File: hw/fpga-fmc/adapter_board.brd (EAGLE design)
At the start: 69 x 84 mm, 5 parts, among them J1 5569262-1, J2 ASP-134488-01

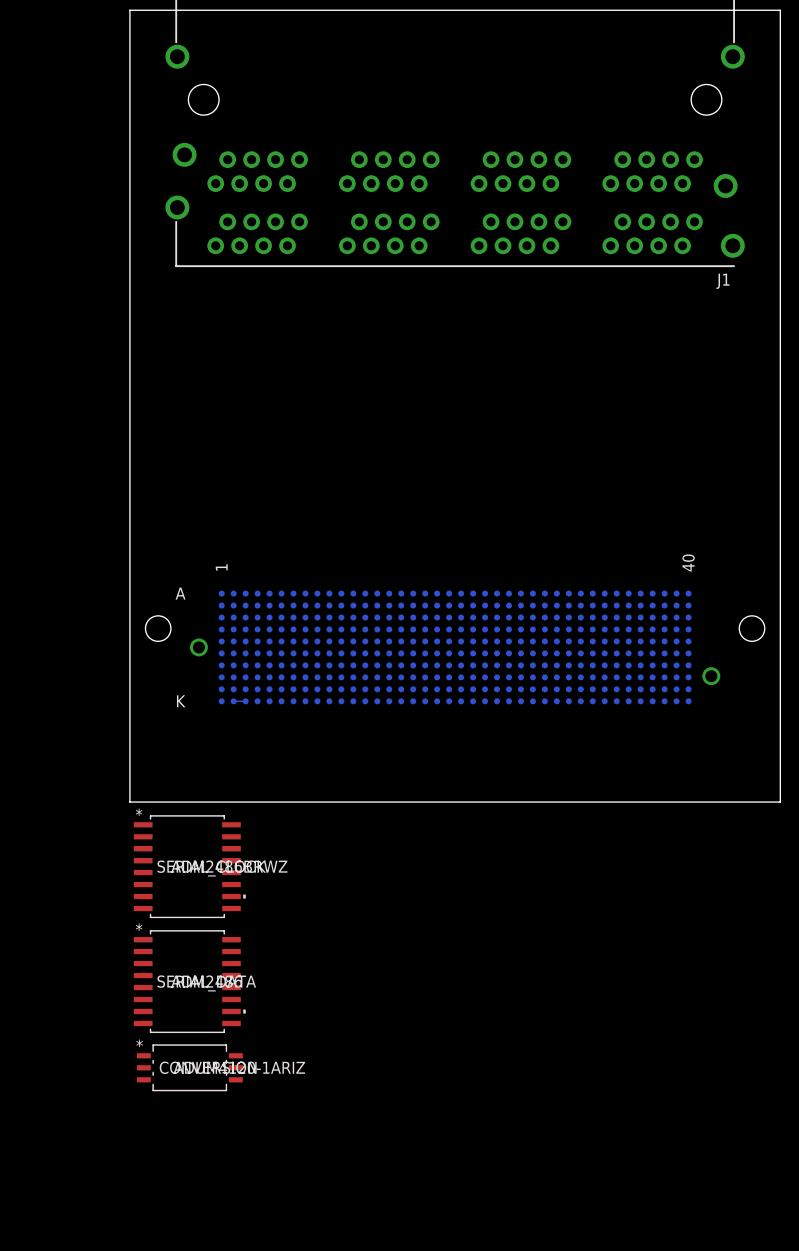
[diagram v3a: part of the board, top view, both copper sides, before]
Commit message: fpga-fmc: add more isolator ics. add i2c switch ic
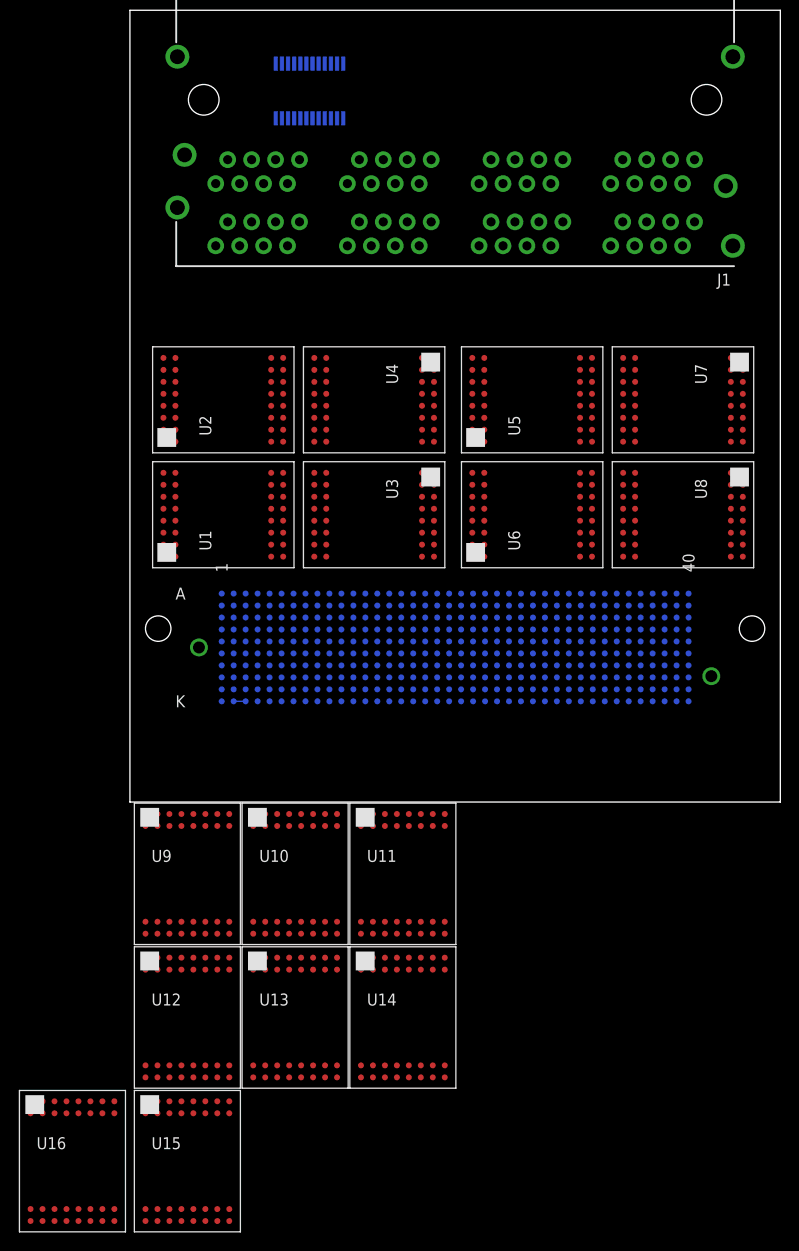
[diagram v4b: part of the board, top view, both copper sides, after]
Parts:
- removed CONVERSION: ADUM4120-1ARIZ, ADUM4120:RI_6_1_ADI
- removed SERIAL_CLOCK: ADM2486BRWZ, ADM2486:RW_16_ADI
- removed SERIAL_DATA: ADM2486, ADM2486:RW_16_ADI
- added U$1: PCA9548A, parts:PCA9548
- added U1, U10, U11, U12, U13, U14, U15, U16, U2, U3, U4, U5, U6, U7, U8, U9: LTM2881, parts:LTM2881-BGA32
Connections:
- removed net N$24: CONVERSION.5
- new net 1V8: U1.A7
- new net N$18: U1.A5
- new net N$19: U1.A2
- new net N$20: U1.A4
- new net N$23: U1.A1
- new net N$25: U1.L7, U1.L8
- new net N$30: U1.L6
- new net N$38: U1.L5
- new net N$41: U1.L3
- new net N$42: U1.L4
- new net N$43: U1.L2
- new net N$44: U1.L1
- new net N$45: U1.K1, U1.K2, U1.K3, U1.K4, U1.K5, U1.K6, U1.K7, U1.K8
- new net U1_ON: U1.A8
- net +3V3: now also U1.B6, U1.B7, U1.B8
- net 0V: now also U1.B1, U1.B2, U1.B3, U1.B4, U1.B5
- net FMC_LA06_N: now also U1.A3
- net FMC_LA06_P: now also U1.A6

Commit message: fpga-fmc: add 4 channel isolator ic
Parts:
- added I2C: ADUM1251, ADUM1251WARZ:R_8_ADI
- added U$2, U$3: ADUM140DQSOP-16, parts:QSOP16
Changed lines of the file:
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@@
 <attribute name="VALUE" x="24.506665625" y="79.248" size="1.27" layer="28" rot="MR270"/>
+</element>
+<element name="I2C" library="ADUM1251WARZ" package="R_8_ADI" value="ADUM1251" x="9.906" y="52.578" smashed="yes" rot="R90">
+<attribute name="BUILT_BY" value="EMA_UL_Team" x="9.906" y="52.578" size="1.778" layer="27" rot="R90" display="off"/>
+<attribute name="COPYRIGHT" value="Copyright (C) 2018 Accelerated Designs. All rights reserved" x="9.906" y="52.578" size="1.778" layer="27" rot="R90" display="off"/>
+<attribute name="DIGIKEY" value="ADUM1251ARZ-RL7TR-ND" x="9.906" y="52.578" size="1.778" layer="27" rot="R90" display="off"/>
+<attribute name="MANUFACTURER_PART_NUMBER" value="ADUM1251WARZ" x="9.906" y="52.578" size="1.778" layer="27" rot="R90" display="off"/>
+<attribute name="NAME" x="10.541" y="49.3014" size="1.27" layer="25" ratio="6" rot="SR90"/>
+<attribute name="SOURCELIBRARY" value="Analog_2019-03-08" x="9.906" y="52.578" size="1.778" layer="27" rot="R90" display="off"/>
+<attribute name="VALUE" x="10.541" y="50.8508" size="1.27" layer="21" ratio="6" rot="SR90"/>
+<attribute name="VENDOR" value="Analog Devices Inc" x="9.906" y="52.578" size="1.778" layer="27" rot="R90" display="off"/>
+</element>
+<element name="U$2" library="parts" package="QSOP16" package3d_urn="urn:adsk.eagle:package:3955/1" value="ADUM140DQSOP-16" x="42.672" y="52.578" smashed="yes">
+<attribute name="NAME" x="39.632" y="50.038" size="1.27" layer="25" rot="R90"/>
+<attribute name="VALUE" x="46.982" y="50.038" size="1.27" layer="27" rot="R90"/>
+</element>
+<element name="U$3" library="parts" package="QSOP16" package3d_urn="urn:adsk.eagle:package:3955/1" value="ADUM140DQSOP-16" x="25.908" y="52.578" smashed="yes">
+<attribute name="NAME" x="22.868" y="50.038" size="1.27" layer="25" rot="R90"/>
+<attribute name="VALUE" x="30.218" y="50.038" size="1.27" layer="27" rot="R90"/>
 </element>
 </elements>
@@
 </drawing>
 <compatibility>
+<note version="8.3" severity="warning">
+Since Version 8.3, EAGLE supports URNs for individual library
+assets (packages, symbols, and devices). The URNs of those assets
+will not be understood (or retained) with this version.
+</note>
+<note version="8.3" severity="warning">
+Since Version 8.3, EAGLE supports the association of 3D packages
+with devices in libraries, schematics, and board files. Those 3D
+packages will not be understood (or retained) with this version.
+</note>
 <note version="8.5" severity="warning">
 Since Version 8.5, EAGLE supports locking for holes, vias, wires and polygons.

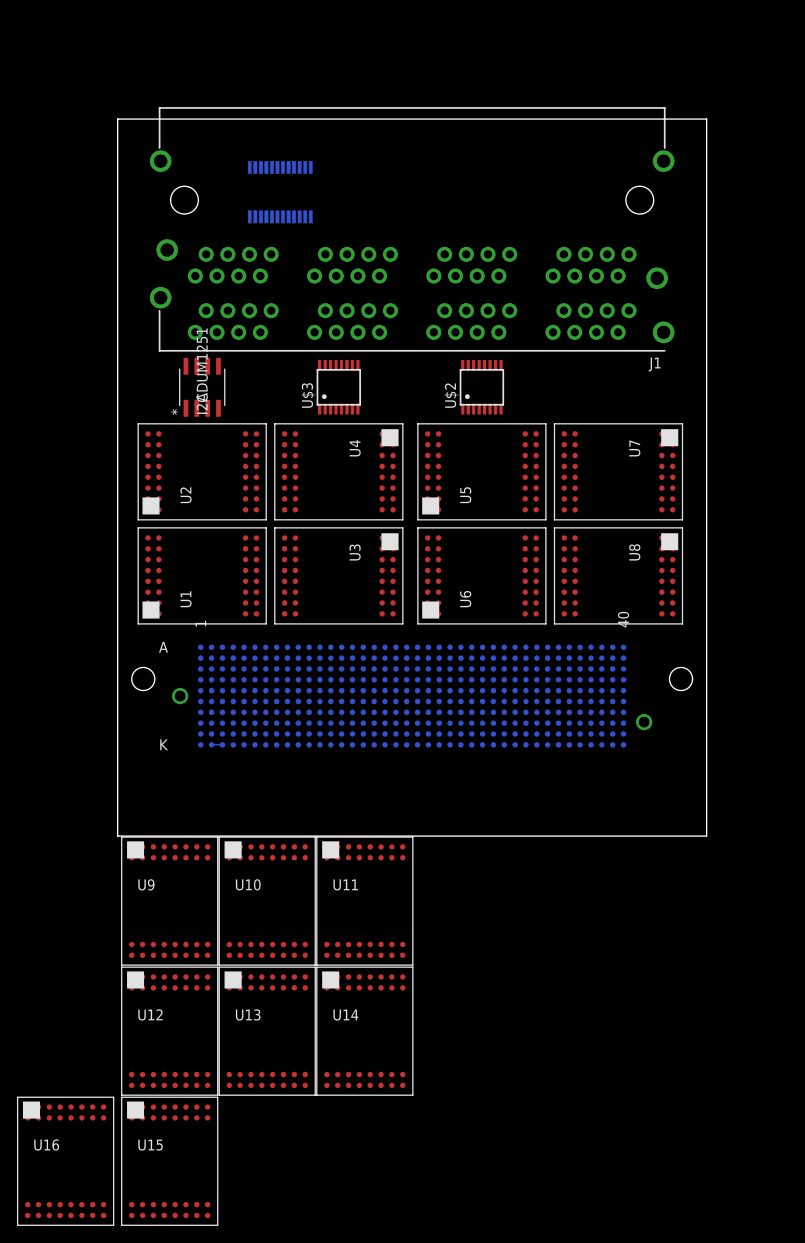
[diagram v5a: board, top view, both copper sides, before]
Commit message: hw/fpga-fmc: add and route rs485 transceiver for 3 channels
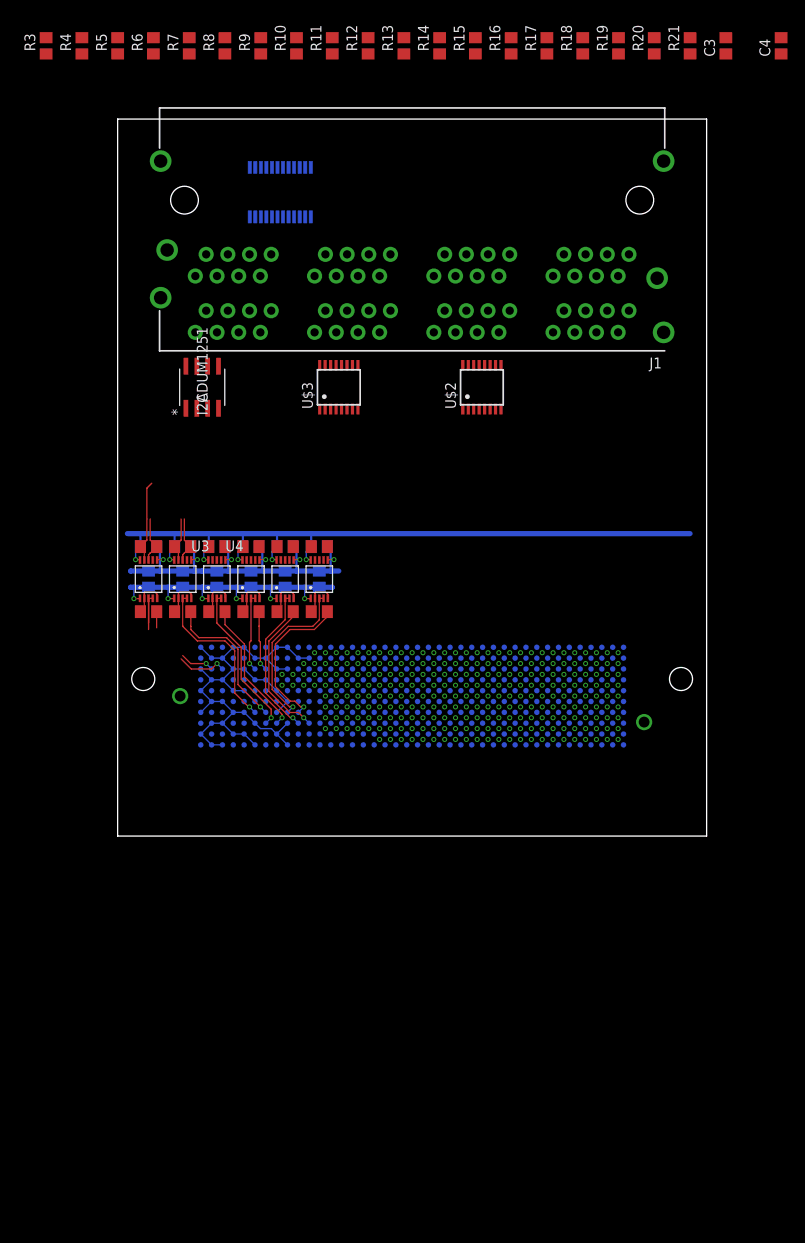
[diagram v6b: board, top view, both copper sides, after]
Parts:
- removed U10, U11, U12, U13, U14, U15, U16, U7, U8, U9: LTM2881, parts:LTM2881-BGA32
- added C1, C10, C11, C12, C13, C14, C2, C3, C5, C6, C7, C8, C9: 100n, rcl:C0805
- added C4: 1u, rcl:C0805
- added R1, R10, R11, R12, R13, R14, R15, R16, R17, R18, R19, R20, R21, R22, R24, R26, R28, R3, R30, R4, R5, R6, R7, R8, R9: (no value), rcl:R0805
- added R2, R23, R25, R27, R29, R31: 100R, rcl:R0805
- U1, U2, U3, U4, U5, U6: value LTM2881 -> ADM3066E; device parts:LTM2881-BGA32 -> parts:MSOP-10
- moved U5 26.3 mm to (19.6, 30.1), turned to 0 degrees
- moved U6 19.1 mm to (23.6, 30.1), turned to 0 degrees
- moved U4 16.2 mm to (15.6, 30.1), turned to 0 degrees
- moved U3 14.3 mm to (11.6, 30.1), turned to 0 degrees
- moved U2 12.8 mm to (7.62, 30.1), turned to 0 degrees
- moved U1 6.30 mm to (3.62, 30.1), turned to 0 degrees
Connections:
- net N$10 renamed RJ6_SDO
- net N$11 renamed RJ6_SCL
- net N$12 renamed RJ6_DATA_P
- net N$13 renamed RJ6_CONV
- net N$15 renamed RJ6_DATA_N
- net N$16 renamed RJ6_CLK_N
- net N$17 renamed RJ6_CLK_P
- net N$2 renamed RJ5_SDO
- net N$26 renamed RJ7_SDO
- net N$27 renamed RJ7_SCL
- net N$29 renamed RJ7_CONV
- net N$3 renamed RJ5_SCL
- net N$34 renamed RJ8_SDO
- net N$35 renamed RJ8_SCL
- net N$37 renamed RJ8_CONV
- net N$4 renamed RJ5_DATA_P
- net N$5 renamed RJ5_CONV
- net N$7 renamed RJ5_DATA_N
- net N$8 renamed RJ5_CLK_N
- net N$9 renamed RJ5_CLK_P
- removed net N$28: J1.7.6
- removed net N$31: J1.7.3
- removed net N$32: J1.7.2
- removed net N$33: J1.7.1
- removed net N$36: J1.8.6
- removed net N$39: J1.8.3
- removed net N$40: J1.8.2
- removed net N$57: J1.8.1
- removed net U1_ON: U1.A8
- new net 3V3: C3.2, C4.2, U$1.P23
- new net 5V: C10.1, C12.1, C14.1, C2.1, C6.1, C8.1, R10.2, R11.2, R12.2, R13.2, R14.2, R15.2, R16.2, R17.2, R18.2, R19.2, R20.2, R21.2, R3.2, R4.2, R8.2, R9.2, U1.P9, U2.P9, U3.P9, U4.P9, U5.P9, U6.P9
- new net LSIO1: R2.1, U1.P1, U1.P4
- new net LSIO2: R23.1, U2.P1, U2.P4
- new net LSIO3: R25.1, U3.P1, U3.P4
- new net LSIO4: R27.1, U4.P1, U4.P4
- new net LSIO5: R29.1, U5.P1, U5.P4
- new net LSIO6: R31.1, U6.P1, U6.P4
- new net N$1: R3.1, U$1.P3
- new net N$14: R8.1, U$1.P5
- new net N$21: U$1.P9
- new net N$22: R12.1, R13.1, U$1.P10
- new net N$24: R15.1, U$1.P13
- new net N$46: R7.1, U$1.P2
- new net N$6: R4.1, U$1.P4
- new net RJ7_CLK_N: J1.7.2, R28.2, U5.P8
- new net RJ7_CLK_P: J1.7.1, R28.1, U5.P7
- new net RJ7_DATA_N: J1.7.3, R30.2, U6.P8
- new net RJ7_DATA_P: J1.7.6, R30.1, U6.P7
- new net RJ8_CLK_N: J1.8.2, R1.2, U1.P8
- new net RJ8_CLK_P: J1.8.1, R1.1, U1.P7
- new net RJ8_DATA_N: J1.8.3, R22.2, U2.P8
- new net RJ8_DATA_P: J1.8.6, R22.1, U2.P7
- net +3V3: no longer U1.B6, U1.B7, U1.B8
- net 0V: now also C1.2, C10.2, C11.2, C12.2, C13.2, C14.2, C2.2, C3.1, C4.1, C5.2, C6.2, C7.2, C8.2, C9.2, U$1.P0, U$1.P1, U$1.P11, U$1.P20, U1.P5, U2.P5, U3.P5, U4.P5, U5.P5, U6.P5; no longer U1.B1, U1.B2, U1.B3, U1.B4, U1.B5
- net 1V8: now also C1.1, C11.1, C13.1, C5.1, C7.1, C9.1, R5.2, R6.2, R7.2, U1.P0, U2.P0, U3.P0, U4.P0, U5.P0, U6.P0; no longer U1.A7
- net FMC_DP0_C2M_N: now also U1.P2, U1.P3
- net FMC_DP0_C2M_P: now also R2.2
- net FMC_DP0_M2C_N: now also R27.2
- net FMC_DP0_M2C_P: now also U4.P2, U4.P3
- net FMC_LA00_CC_N: now also R23.2
- net FMC_LA00_CC_P: now also U2.P2, U2.P3
- net FMC_LA02_N: now also R25.2
- net FMC_LA02_P: now also U3.P2, U3.P3
- net FMC_LA03_N: now also R31.2
- net FMC_LA03_P: now also U6.P2, U6.P3
- net FMC_LA04_N: now also R29.2
- net FMC_LA04_P: now also U5.P2, U5.P3
- net FMC_LA06_N: no longer U1.A3
- net FMC_LA06_P: no longer U1.A6
- net N$18: now also R9.1, U$1.P6; no longer U1.A5
- net N$19: now also R10.1, U$1.P7; no longer U1.A2
- net N$20: now also R11.1, U$1.P8; no longer U1.A4
- net N$23: now also R14.1, U$1.P12; no longer U1.A1
- net N$25: now also R16.1, U$1.P14; no longer U1.L7, U1.L8
- net N$30: now also R17.1, U$1.P15; no longer U1.L6
- net N$38: now also R18.1, U$1.P16; no longer U1.L5
- net N$41: now also R19.1, U$1.P17; no longer U1.L3
- net N$42: now also R20.1, U$1.P18; no longer U1.L4
- net N$43: now also R21.1, U$1.P19; no longer U1.L2
- net N$44: now also R5.1, U$1.P22; no longer U1.L1
- net N$45: now also R6.1, U$1.P21; no longer U1.K1, U1.K2, U1.K3, U1.K4, U1.K5, U1.K6, U1.K7, U1.K8
- net RJ4_CLK_N: now also R24.2, U3.P8
- net RJ4_CLK_P: now also R24.1, U3.P7
- net RJ4_DATA_N: now also R26.2, U4.P8
- net RJ4_DATA_P: now also R26.1, U4.P7
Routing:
- net 0V: track 1.27 -> 119.9 mm, vias 0 -> 6
- net 5V: track 0.00 -> 89.0 mm, vias 0 -> 6
- net 1V8: track 0.00 -> 36.0 mm, vias 0 -> 6
- net FMC_LA00_CC_P: track 0.00 -> 19.3 mm, vias 0 -> 1
- net FMC_LA03_P: track 0.00 -> 19.3 mm, vias 0 -> 1
- net FMC_LA03_N: track 0.00 -> 18.2 mm, vias 0 -> 1
- net FMC_LA02_P: track 0.00 -> 18.0 mm, vias 0 -> 1
- net FMC_LA04_P: track 0.00 -> 17.8 mm, vias 0 -> 1
- net FMC_LA00_CC_N: track 0.00 -> 17.3 mm, vias 0 -> 1
- net FMC_LA04_N: track 0.00 -> 16.8 mm, vias 0 -> 1
- net FMC_LA02_N: track 0.00 -> 16.1 mm, vias 0 -> 1
- net FMC_DP0_C2M_N: track 0.00 -> 12.9 mm, vias 0 -> 1
- net RJ8_CLK_N: track 0.00 -> 9.75 mm
- net FMC_DP0_M2C_P: track 0.00 -> 9.11 mm, vias 0 -> 1
- net FMC_DP0_M2C_N: track 0.00 -> 7.04 mm, vias 0 -> 1
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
